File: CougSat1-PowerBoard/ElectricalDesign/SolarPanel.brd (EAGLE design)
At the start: 80 x 97 mm, 112 parts, among them J1 Wire Harness Connector, U1 SPV1040, U2 SPV1040, U3 TCA9535R, U4 LTC2499, U5 LTC2499, U6 MCP1501-18

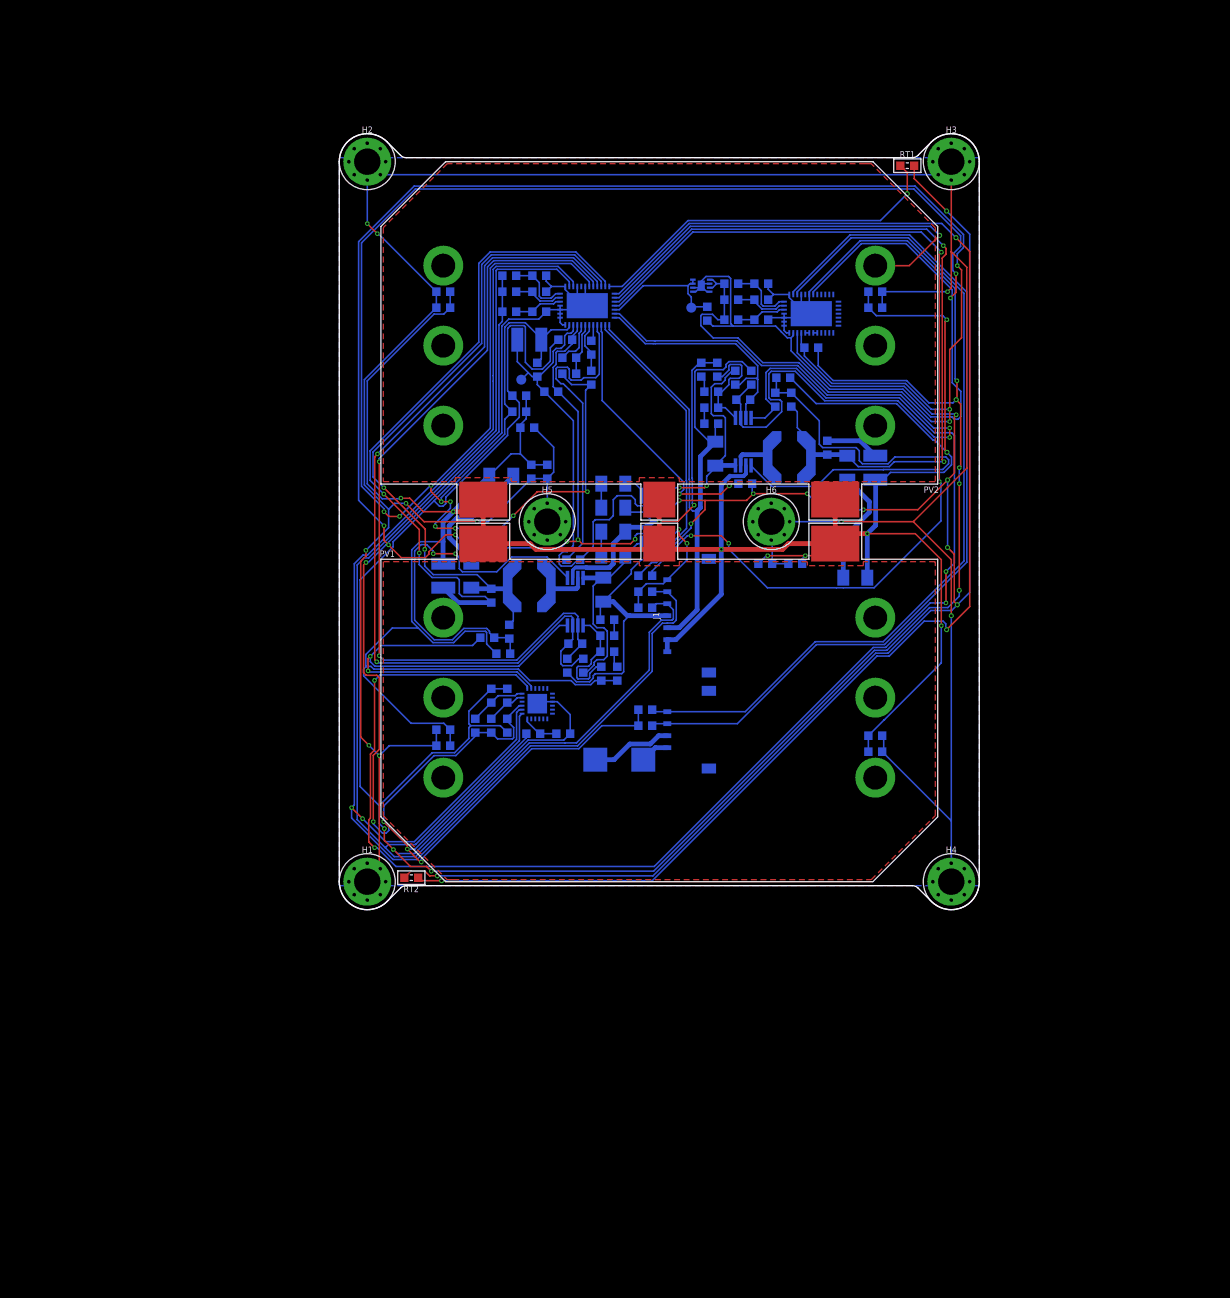
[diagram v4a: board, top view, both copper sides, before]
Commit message: Addded Photodiode, Moved Holes
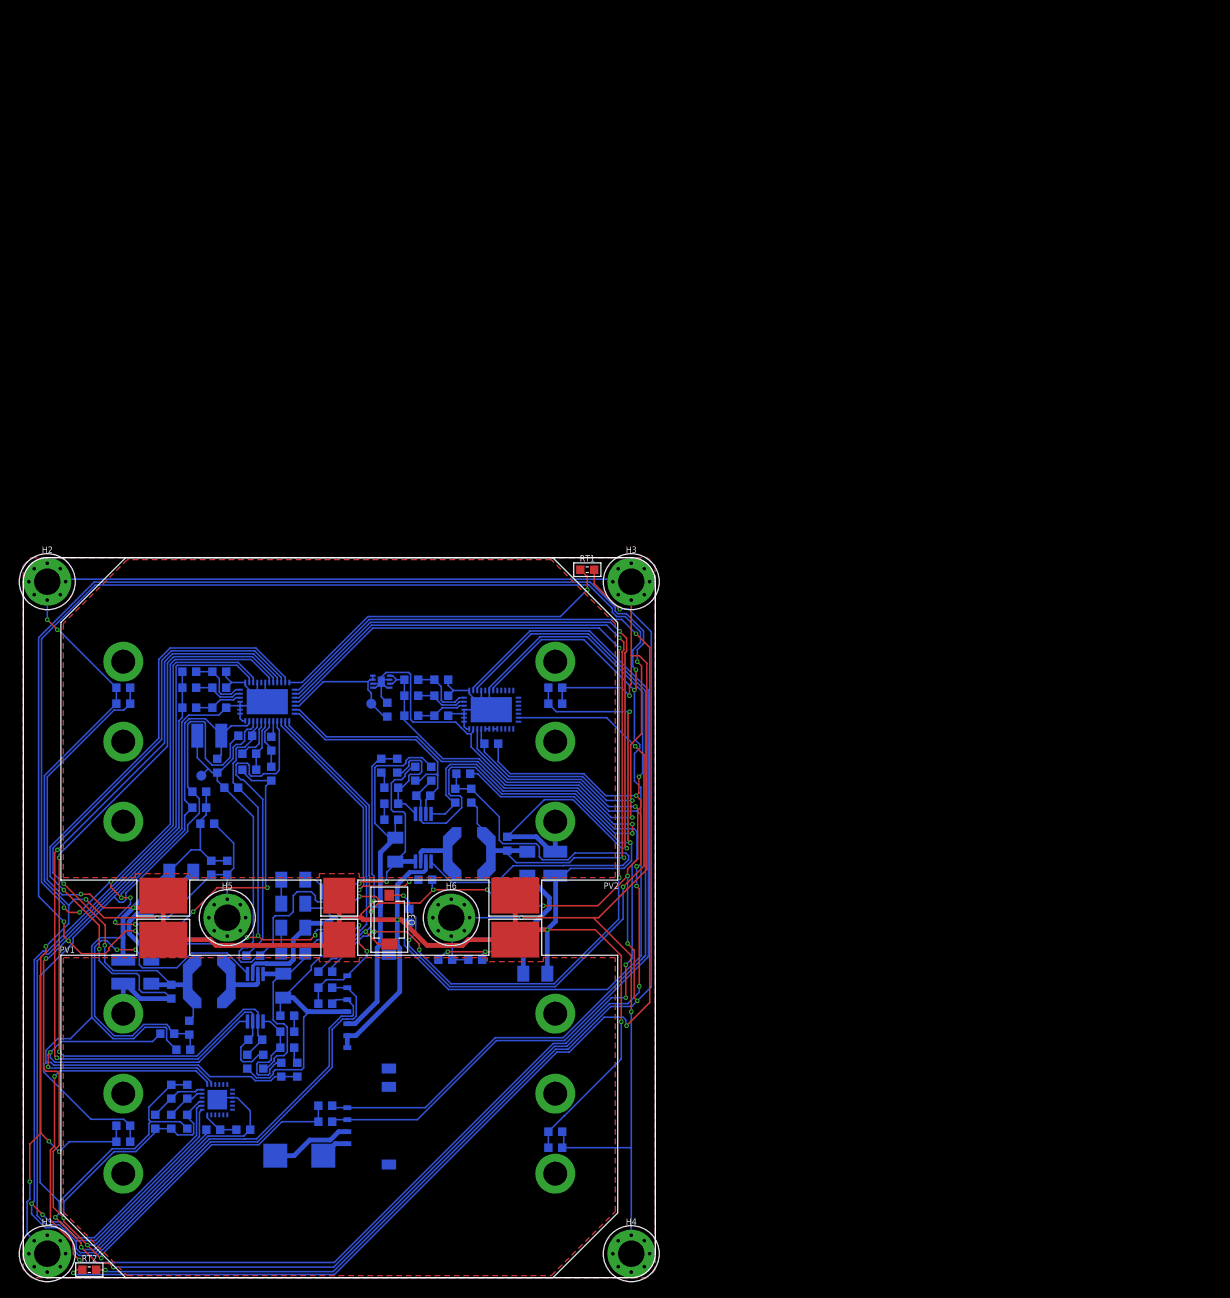
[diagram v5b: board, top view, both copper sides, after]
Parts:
- added D3: SFH 2430, CougsInSpace-Sensors:SFH2430
- added R56: 150Ω 1%, CougsInSpace-Resistors:1608
- moved H2 66.0 mm to (-36.5, 42.0)
- moved H3 66.0 mm to (36.5, 42.0)
- moved RT1 64.4 mm to (31.0, 43.5)
- moved C1 63.6 mm to (-27.0, -6.75)
- moved C10 63.6 mm to (15.5, 18.0)
- moved C11 63.6 mm to (-5.75, 4.75)
- moved C12 63.6 mm to (10.5, 15.2)
- moved C13 63.6 mm to (7.25, 19.0)
- moved C14 63.6 mm to (-5.75, 1.75)
- moved C15 63.6 mm to (6.00, 26.0), turned to 90 degrees
- moved C16 63.6 mm to (-19.0, -25.5)
- moved C17 63.6 mm to (-11.8, 22.8)
- moved C18 63.6 mm to (-16.2, 22.8)
- moved C19 63.6 mm to (-15.2, 19.0)
- moved C2 63.6 mm to (-23.5, -6.75)
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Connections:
- new net PHOTODIODE: D3.A, R56.2, U5.18
- net AGND: now also R56.1
- net AVDD: now also D3.C
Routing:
- net PHOTODIODE: track 0.00 -> 80.6 mm, vias 0 -> 4
- net AGND: track 354.8 -> 408.2 mm
- net PV_IIN_P-B: track 63.8 -> 102.4 mm, vias 1 -> 2
- net CHASSIS: track 465.1 -> 453.1 mm, vias 10 -> 11
- net 3.3V: track 477.2 -> 466.5 mm, vias 16 -> 15
- net TEMP_FRONT_TOP: track 178.6 -> 182.7 mm
- net PV_IIN_N-B: track 98.3 -> 100.8 mm
- net AVDD: track 308.8 -> 310.6 mm, vias 11 -> 12
- net TEMP_FRONT_BOTTOM: track 45.9 -> 44.9 mm
- net I2C_SCL_PMIC: track 173.3 -> 172.3 mm
- net PV_IIN_P-A: track 86.0 -> 86.9 mm
- net PGND: track 430.8 -> 429.9 mm
- net DGND: track 399.5 -> 400.3 mm
- net !MPPT_XSHUT-B: track 185.3 -> 184.5 mm
- net MPPT_ICTRL_N-B: track 93.3 -> 93.9 mm
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- added copper zone on layer 1, net BALANCING1
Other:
- board size 80 x 97 mm -> 79 x 90 mm

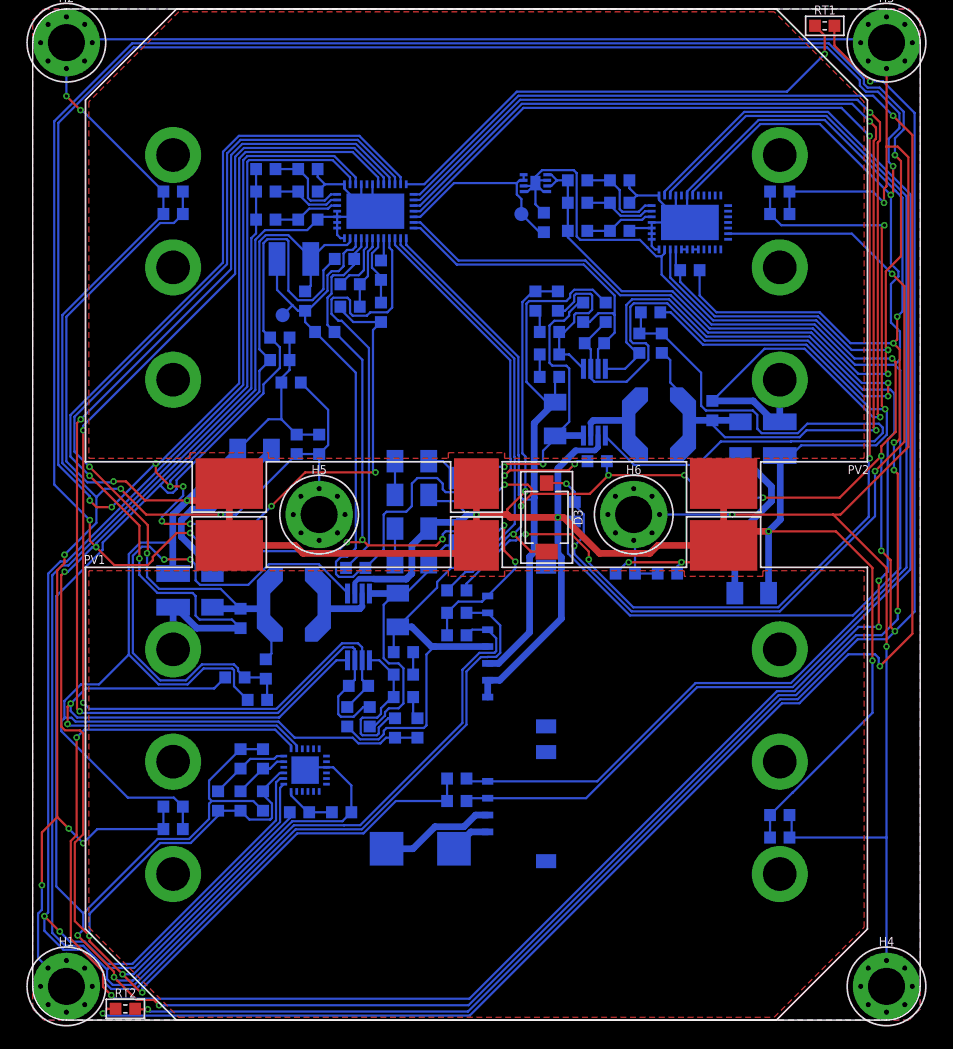
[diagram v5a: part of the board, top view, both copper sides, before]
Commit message: Moved Mounting Hole Capacitors
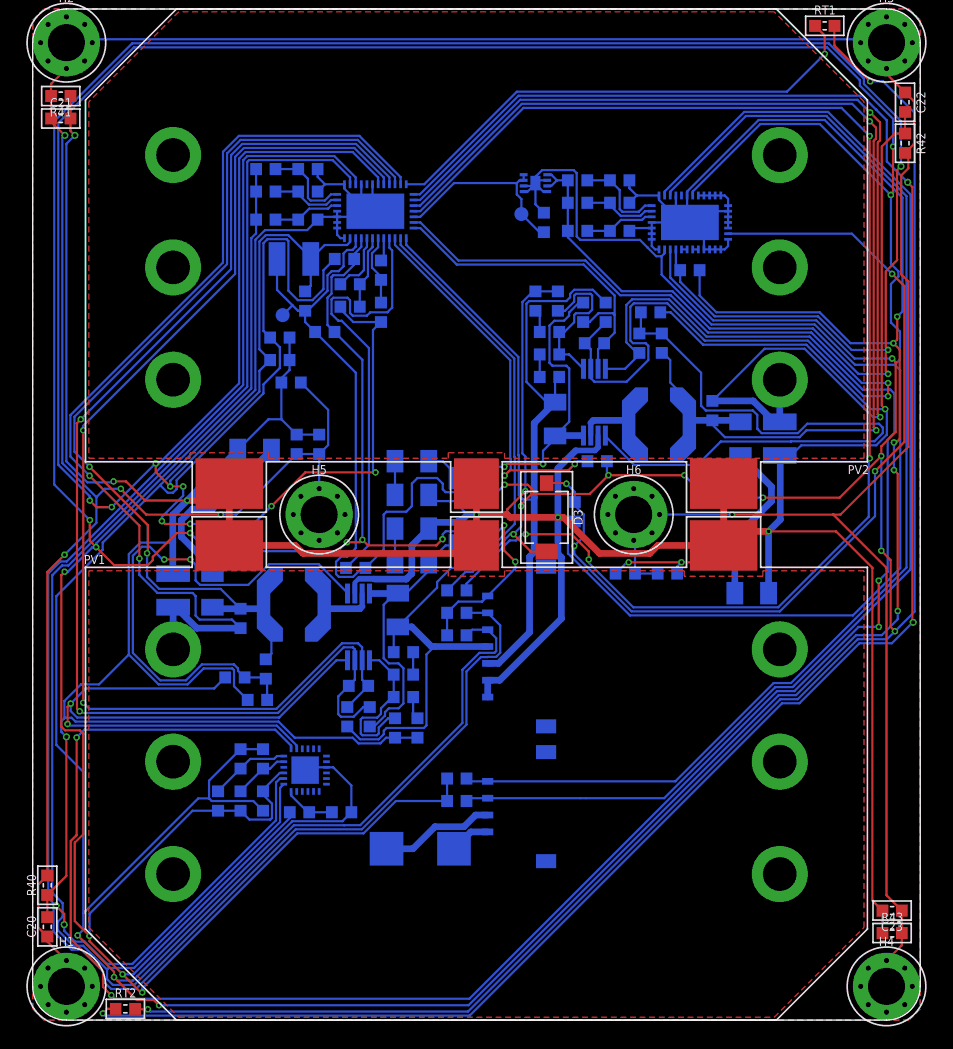
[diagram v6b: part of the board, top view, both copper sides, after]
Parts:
- moved C20 15.5 mm to (-38.2, -36.7), flipped to the top, turned to 90 degrees
- moved C22 14.9 mm to (38.1, 36.7), flipped to the top, turned to 270 degrees
- moved C21 13.1 mm to (-37.0, 35.2), flipped to the top, turned to 0 degrees
- moved C23 13.1 mm to (37.0, -35.2), flipped to the top, turned to 180 degrees
- moved R41 13.1 mm to (-37.0, 37.2), flipped to the top, turned to 180 degrees
- moved R43 13.1 mm to (37.0, -37.2), flipped to the top, turned to 0 degrees
- moved R40 12.3 mm to (-38.2, -33.0), flipped to the top, turned to 90 degrees
- moved R42 12.0 mm to (38.1, 33.0), flipped to the top, turned to 270 degrees
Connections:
- net DGND: now also U5.10, U5.11, U5.12, U5.13, U5.14, U5.15, U5.16, U5.17, U5.19, U5.20, U5.21, U5.22, U5.23, U5.8, U5.9
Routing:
- net CHASSIS: track 453.1 -> 406.3 mm, vias 11 -> 5
- net DGND: track 400.3 -> 414.4 mm
- net PGND: track 429.9 -> 439.6 mm
- net TEMP_FRONT_TOP: track 182.7 -> 180.3 mm
- net 3.3V: track 466.5 -> 465.0 mm
- net AGND: track 408.2 -> 406.7 mm

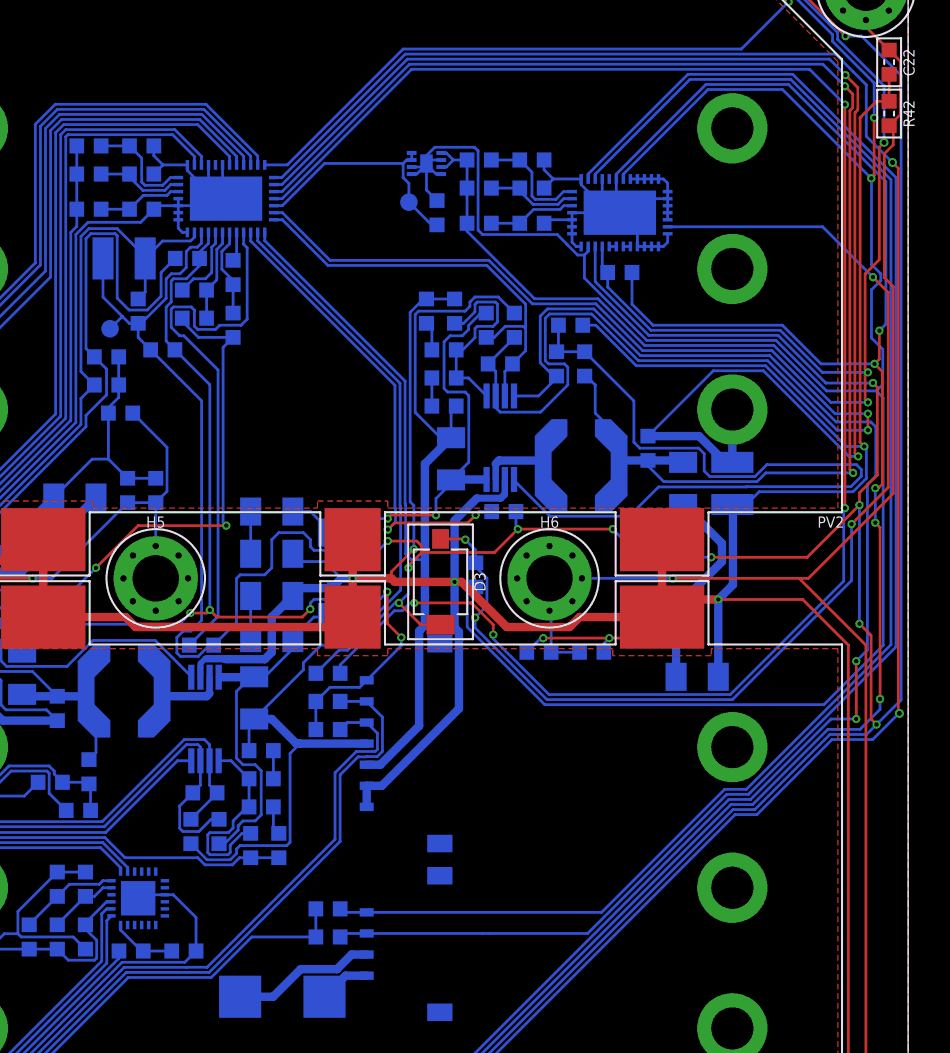
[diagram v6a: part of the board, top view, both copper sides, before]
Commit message: Length Matched I2C
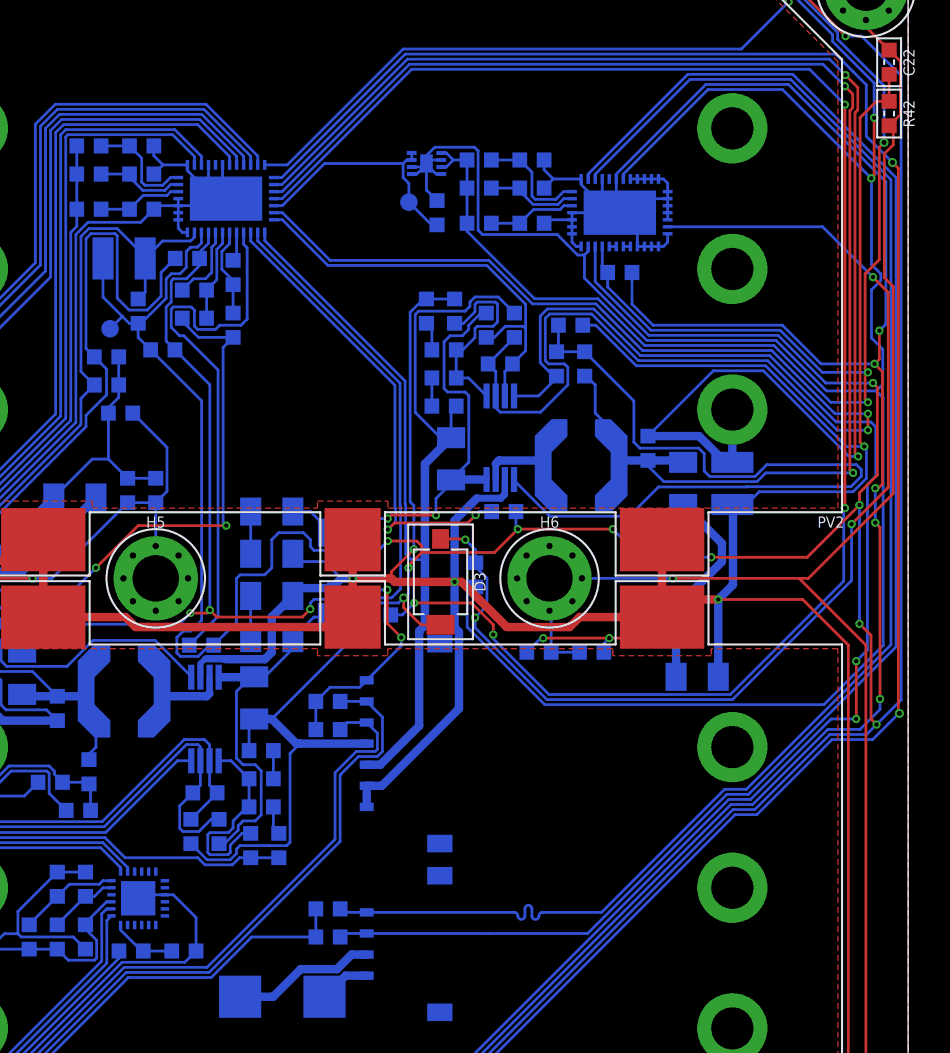
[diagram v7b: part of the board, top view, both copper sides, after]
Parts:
- moved RT3 5.49 mm to (1.85, -2.60)
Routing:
- net TEMP_BACK: track 124.2 -> 118.6 mm
- net AVDD: track 310.6 -> 306.6 mm
- net I2C_SDA_ADCS: track 107.3 -> 108.5 mm
